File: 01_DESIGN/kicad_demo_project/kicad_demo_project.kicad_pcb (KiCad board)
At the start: 2 copper layers, 15 parts, among them J1 JP2, J2 0473460001, J3 JP8, J4 JP2, J5 JP8, U2 TPS7A4533DCQR, U3 STM32H745ZIT3, U6 ATMEGA324PA, U8 LM2596S-5, Y1 ECS-250-12-33Q-JES-TR, Y2 8MHz

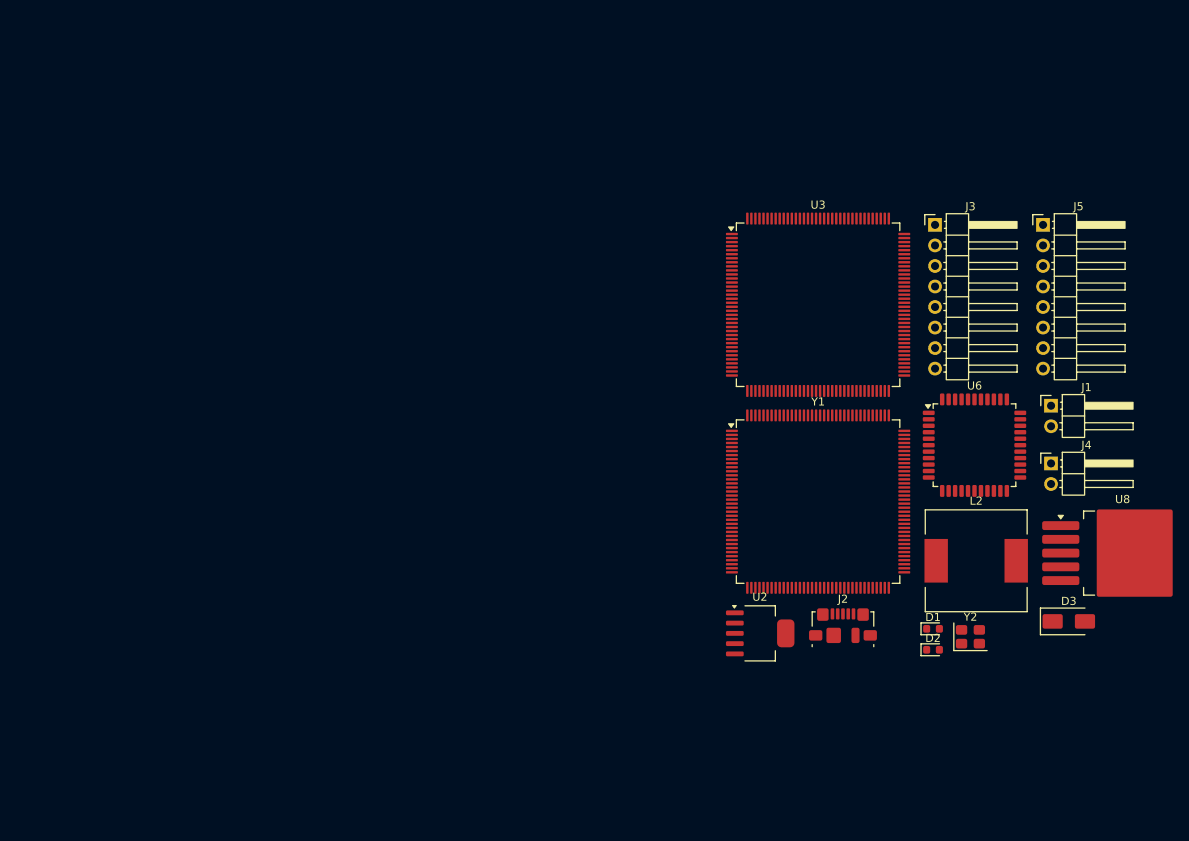
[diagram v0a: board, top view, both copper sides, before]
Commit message: Update schematic, PCB
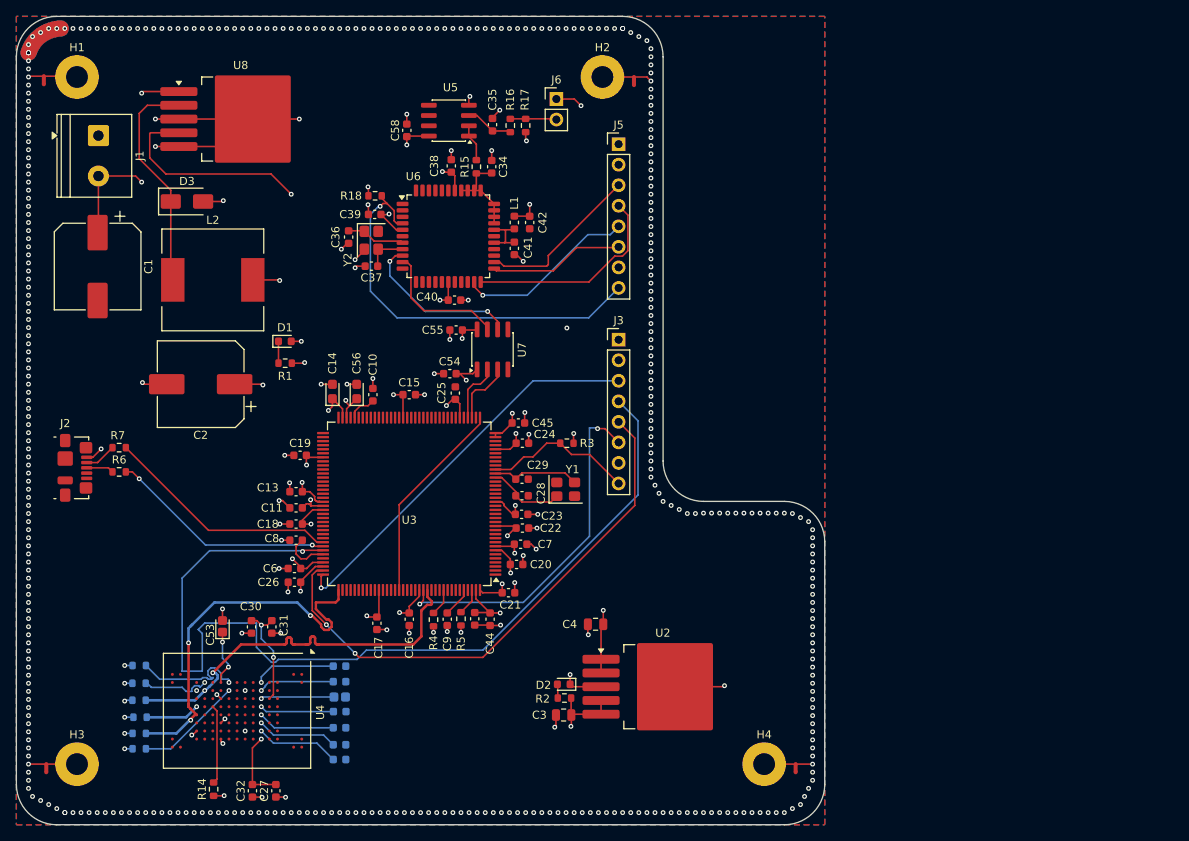
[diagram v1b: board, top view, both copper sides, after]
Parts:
- removed J4: JP2, Connector_PinHeader_2.54mm:PinHeader_1x02_P2.54mm_Horizontal
- added C1: 680uF, Capacitor_SMD:CP_Elec_10x10.5, F.Cu at (60.0, 74.0)
- added C10: 4.7uF/6.3V, Capacitor_SMD:C_0603_1608Metric, F.Cu at (94.1, 89.8)
- added C11: 0.1uF/6.3V, Capacitor_SMD:C_0603_1608Metric, F.Cu at (84.6, 103.8)
- added C13: 4.7uF/6.3V, Capacitor_SMD:C_0603_1608Metric, F.Cu at (84.6, 101.8)
- added C14: 4.7uF, Capacitor_Tantalum_SMD:CP_EIA-2012-15_AVX-P, F.Cu at (89.1, 89.4)
- added C15: 0.1uF/6.3V, Capacitor_SMD:C_0603_1608Metric, F.Cu at (98.6, 89.8)
- added C16: 0.1uF/6.3V, Capacitor_SMD:C_0603_1608Metric, F.Cu at (98.6, 117.6)
- added C17: 0.1uF/6.3V, Capacitor_SMD:C_0603_1608Metric, F.Cu at (94.6, 118.1)
- added C18: 0.1uF/6.3V, Capacitor_SMD:C_0603_1608Metric, F.Cu at (84.6, 105.8)
- added C19: 0.1uF/6.3V, Capacitor_SMD:C_0603_1608Metric, F.Cu at (85.1, 97.3)
- added C2: 220uF, Capacitor_SMD:CP_Elec_10x10.5, F.Cu at (72.8, 88.5)
- added C20: 0.1uF/6.3V, Capacitor_SMD:C_0603_1608Metric, F.Cu at (111.9, 110.8)
- added C21: 0.1uF/6.3V, Capacitor_SMD:C_0603_1608Metric, F.Cu at (110.9, 114.3)
- added C22: 0.1uF/6.3V, Capacitor_SMD:C_0603_1608Metric, F.Cu at (112.6, 106.3)
- added C23: 0.1uF/6.3V, Capacitor_SMD:C_0603_1608Metric, F.Cu at (112.5, 104.6)
- added C24: 0.1uF/6.3V, Capacitor_SMD:C_0603_1608Metric, F.Cu at (112.6, 95.8)
- added C25: 0.1uF/6.3V, Capacitor_SMD:C_0603_1608Metric, F.Cu at (104.3, 89.6)
- added C26: 0.1uF/6.3V, Capacitor_SMD:C_0603_1608Metric, F.Cu at (84.4, 113.0)
- added C27: 0.1uF/6.3V, Capacitor_SMD:C_0603_1608Metric, F.Cu at (82.1, 138.8)
- added C28: 16pF/6.3V, Capacitor_SMD:C_0603_1608Metric, F.Cu at (112.5, 102.3)
- added C29: 16pF/6.3V, Capacitor_SMD:C_0603_1608Metric, F.Cu at (112.5, 100.2)
- added C3: 10uF, Capacitor_SMD:C_0805_2012Metric, F.Cu at (117.7, 129.4)
- added C30: 0.1uF/6.3V, Capacitor_SMD:C_0603_1608Metric, F.Cu at (79.1, 118.5)
- added C31: 1uF/6.3V, Capacitor_SMD:C_0603_1608Metric, F.Cu at (81.6, 118.5)
- added C32: 0.1uF/6.3V, Capacitor_SMD:C_0603_1608Metric, F.Cu at (79.2, 138.8)
- added C34: 0.1uF/6.3V, Capacitor_SMD:C_0603_1608Metric, F.Cu at (108.8, 61.6)
- added C35: 0.1uF/6.3V, Capacitor_SMD:C_0603_1608Metric, F.Cu at (108.9, 56.4)
- added C36: 16pF/6.3V, Capacitor_SMD:C_0603_1608Metric, F.Cu at (91.1, 70.3)
- added C37: 16pF/6.3V, Capacitor_SMD:C_0603_1608Metric, F.Cu at (93.9, 73.9)
- added C38: 0.1uF/6.3V, Capacitor_SMD:C_0603_1608Metric, F.Cu at (103.8, 61.5)
- added C39: 0.1uF/6.3V, Capacitor_SMD:C_0603_1608Metric, F.Cu at (94.3, 67.5)
- added C4: 10uF, Capacitor_SMD:C_0805_2012Metric, F.Cu at (121.7, 118.2)
- added C40: 0.1uF/6.3V, Capacitor_SMD:C_0603_1608Metric, F.Cu at (104.2, 78.1)
- added C41: 0.1uF/6.3V, Capacitor_SMD:C_0603_1608Metric, F.Cu at (111.6, 71.7)
- added C42: 0.1uF/6.3V, Capacitor_SMD:C_0603_1608Metric, F.Cu at (113.5, 68.5)
- added C43: 0.1uF/6.3V, Capacitor_SMD:CAP_C_1608X80, F.Cu at (106.7, 117.5)
- added C44: 0.1uF/6.3V, Capacitor_SMD:C_0603_1608Metric, F.Cu at (108.6, 117.6)
- added C45: 0.1uF/6.3V, Capacitor_SMD:C_0603_1608Metric, F.Cu at (112.1, 93.3)
- added C46: 0.1uF/6.3V, Capacitor_SMD:C_0603_1608Metric, B.Cu at (90.0, 134.9)
- added C47: 0.1uF/6.3V, Capacitor_SMD:C_0603_1608Metric, B.Cu at (90.0, 133.1)
- added C48: 0.1uF/6.3V, Capacitor_SMD:C_0603_1608Metric, B.Cu at (90.0, 131.0)
- added C49: 0.1uF/6.3V, Capacitor_SMD:C_0603_1608Metric, B.Cu at (90.0, 129.0)
- added C50: 0.1uF/6.3V, Capacitor_SMD:C_0603_1608Metric, B.Cu at (90.0, 125.3)
- added C51: 0.1uF/6.3V, Capacitor_SMD:C_0603_1608Metric, B.Cu at (90.0, 123.4)
- added C52: 4.7uF, Capacitor_Tantalum_SMD:CP_EIA-1608-10_AVX-L, B.Cu at (90.0, 127.2)
- added C53: 4.7uF, Capacitor_Tantalum_SMD:CP_EIA-1608-10_AVX-L, F.Cu at (75.5, 118.5)
- added C54: 0.1uF/6.3V, Capacitor_SMD:C_0603_1608Metric, F.Cu at (103.6, 87.2)
- added C55: 0.1uF/6.3V, Capacitor_SMD:C_0603_1608Metric, F.Cu at (104.4, 81.8)
- added C56: 4.7uF, Capacitor_Tantalum_SMD:CP_EIA-2012-15_AVX-P, F.Cu at (92.1, 89.4)
- added C58: 0.1uF/6.3V, Capacitor_SMD:C_0603_1608Metric, F.Cu at (98.3, 57.1)
- added C6: 0.1uF/6.3V, Capacitor_SMD:C_0603_1608Metric, F.Cu at (84.4, 111.3)
- added C7: 0.1uF/6.3V, Capacitor_SMD:C_0603_1608Metric, F.Cu at (112.4, 108.3)
- added C8: 4.7uF/6.3V, Capacitor_SMD:C_0603_1608Metric, F.Cu at (84.6, 107.8)
- added C9: 4.7uF/6.3V, Capacitor_SMD:C_0603_1608Metric, F.Cu at (103.3, 117.6)
- added H1: MountingHole_Pad, MountingHole:MountingHole_2.7mm_M2.5_Pad, F.Cu at (57.5, 50.5)
- added H2: MountingHole_Pad, MountingHole:MountingHole_2.7mm_M2.5_Pad, F.Cu at (122.5, 50.5)
- added H3: MountingHole_Pad, MountingHole:MountingHole_2.7mm_M2.5_Pad, F.Cu at (57.5, 135.5)
- added H4: MountingHole_Pad, MountingHole:MountingHole_2.7mm_M2.5_Pad, F.Cu at (142.5, 135.5)
- added J6: Conn_01x02, Connector_PinHeader_2.54mm:PinHeader_1x02_P2.54mm_Vertical, F.Cu at (116.8, 53.2)
- added L1: 10uH/250mA, Inductor_SMD:L_0603_1608Metric, F.Cu at (111.6, 68.5)
- added NT1: NetTie_2, NetTie:NetTie-2_SMD_Pad0.5mm, F.Cu at (53.4, 50.9)
- added NT2: NetTie_2, NetTie:NetTie-2_SMD_Pad0.5mm, F.Cu at (126.4, 51.0)
- added NT3: NetTie_2, NetTie:NetTie-2_SMD_Pad0.5mm, F.Cu at (53.7, 136.0)
- added NT4: NetTie_2, NetTie:NetTie-2_SMD_Pad0.5mm, F.Cu at (146.4, 136.0)
- added R1: 1k, Resistor_SMD:R_0603_1608Metric, F.Cu at (83.2, 85.9)
- added R10: 10k, Resistor_SMD:R_0603_1608Metric, B.Cu at (65.2, 125.5)
- added R11: 10k, Resistor_SMD:R_0603_1608Metric, B.Cu at (65.2, 123.3)
- added R12: 10k, Resistor_SMD:R_0603_1608Metric, B.Cu at (65.3, 129.7)
- added R13: 10k, Resistor_SMD:R_0603_1608Metric, B.Cu at (65.2, 131.7)
- added R14: 4.7k, Resistor_SMD:R_0603_1608Metric, F.Cu at (74.4, 138.6)
- added R15: 22R, Resistor_SMD:R_0603_1608Metric, F.Cu at (106.9, 61.6)
- added R16: 22R, Resistor_SMD:R_0603_1608Metric, F.Cu at (111.1, 56.5)
- added R17: 10k, Resistor_SMD:R_0603_1608Metric, F.Cu at (113.0, 56.5)
- added R18: 4.7k, Resistor_SMD:R_0603_1608Metric, F.Cu at (94.4, 65.2)
- added R2: 1k, Resistor_SMD:R_0603_1608Metric, F.Cu at (117.8, 127.3)
- added R3: 4.7k, Resistor_SMD:R_0603_1608Metric, F.Cu at (118.1, 95.8)
- added R4: 4.7k, Resistor_SMD:R_0603_1608Metric, F.Cu at (101.6, 117.6)
- added R5: 4.7k, Resistor_SMD:R_0603_1608Metric, F.Cu at (105.0, 117.5)
- added R6: 0R/DNP, Resistor_SMD:R_0603_1608Metric, F.Cu at (62.7, 99.3)
- added R7: 0R/DNP, Resistor_SMD:R_0603_1608Metric, F.Cu at (62.7, 96.3)
- added R8: 10k, Resistor_SMD:R_0603_1608Metric, B.Cu at (65.2, 127.6)
- added R9: 10k, Resistor_SMD:R_0603_1608Metric, B.Cu at (65.2, 133.6)
- added U4: MTFC32GAZAQDW-AAT, Package_BGA:BGA-100_14x18mm_Layout10x17_P1mm, F.Cu at (77.3, 128.9)
- added U5: OPA2340, Package_SO:SOIC-8_3.9x4.9mm_P1.27mm, F.Cu at (103.5, 55.9)
- added U7: ISO7721DR, Package_SO:SOIC-8_3.9x4.9mm_P1.27mm, F.Cu at (108.9, 84.2)
- J1: value JP2 -> Screw_Terminal_01x02; footprint Connector_PinHeader_2.54mm:PinHeader_1x02_P2.54mm_Horizontal -> TerminalBlock_Phoenix:TerminalBlock_Phoenix_PT-1,5-2-5.0-H_1x02_P5.00mm_Horizontal
- J3, J5: value JP8 -> Conn_01x08; footprint Connector_PinHeader_2.54mm:PinHeader_1x08_P2.54mm_Horizontal -> Connector_PinHeader_2.54mm:PinHeader_1x08_P2.54mm_Vertical
- U2: footprint Package_TO_SOT_SMD:SOT-223-6 -> Package_TO_SOT_SMD:TO-263-5_TabPin3
- Y1: value ECS-250-12-33Q-JES-TR -> Crystal_GND24; footprint Package_QFP:LQFP-144_20x20mm_P0.5mm -> Crystal:Crystal_SMD_3225-4Pin_3.2x2.5mm
- Y2: value 8MHz -> Crystal_GND24
- moved J1 122.5 mm to (60.1, 57.8), turned to -90 degrees
- moved U8 121.6 mm to (77.8, 55.7)
- moved D3 120.8 mm to (71.1, 65.9)
- moved L2 100.6 mm to (74.3, 75.6)
- moved J2 97.0 mm to (57.2, 98.8), turned to -90 degrees
- moved Y2 88.9 mm to (93.9, 70.7), turned to -90 degrees
- moved D1 87.7 mm to (83.2, 83.2)
- moved U6 70.0 mm to (103.4, 70.2)
- moved U3 56.3 mm to (98.6, 103.3), turned to 180 degrees
- moved J5 53.4 mm to (124.5, 58.8)
- moved D2 45.9 mm to (117.7, 125.6), turned to 180 degrees
- moved J3 41.6 mm to (124.5, 83.0)
- moved Y1 31.3 mm to (118.0, 101.5)
- moved U2 13.7 mm to (130.0, 125.9)
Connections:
- J1 pad 1: +12V -> GND
- J1 pad 2: GND -> +12V
- J2 pad SH: (no net) -> unconnected-(J2-Shield-PadSH)_1
- L2 pad 2: Net-(C2-Pad1) -> +5V
- U3 pad 109: unconnected-(U3B-PC10-Pad109) -> MCU_eMMC_SDMMC2_CK
- U3 pad 131: /MCU/MCU_eMMC_SDMMC2_D3 -> MCU_eMMC_SDMMC2_D3
- U3 pad 29: /MCU/MCU_eMMC_SDMMC2_CK -> unconnected-(U3B-PC1-Pad29)
- U3 pad 37: /MCU/MCU_eMMC_SDMMC2_CMD -> /MCU/MCU_eMMC_SDMMC2_D2
- U3 pad 39: /MCU/MCU_ISO_UART2_TX -> MCU_ISO_UART2_TX
- U3 pad 40: /MCU/MCU_ISO_UART2_RX -> MCU_ISO_UART2_RX
- U6 pad 10: /AVR/AVR_ISO_UART0_TX -> AVR_ISO_UART0_TX
- U6 pad 9: /AVR/AVR_ISO_UART0_RX -> AVR_ISO_UART0_RX
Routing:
- net /POWER/SHIELDING: track 0.00 -> 1364.3 mm, vias 0 -> 381
- net +3.3V: track 0.00 -> 195.5 mm, vias 0 -> 48
- net /MCU/MCU_JTAG_TMS: track 0.00 -> 118.0 mm, vias 0 -> 1
- net +5V: track 0.00 -> 107.3 mm, vias 0 -> 15
- net GND: track 0.00 -> 105.2 mm, vias 0 -> 52
- net /MCU/MCU_JTAG_TCK: track 0.00 -> 67.3 mm, vias 0 -> 2
- net /AVR/AVR_JTAG_nRESET: track 0.00 -> 50.3 mm, vias 0 -> 1
- net /MCU/MCU_JTAG_TDI: track 0.00 -> 49.2 mm, vias 0 -> 1
- net MCU_eMMC_SDMMC2_D3: track 0.00 -> 48.4 mm, vias 0 -> 2
- net MCU_eMMC_SDMMC2_CK: track 0.00 -> 47.6 mm, vias 0 -> 3
- net /MCU/MCU_JTAG_TDO: track 0.00 -> 44.1 mm, vias 0 -> 2
- net /MCU/USB_2.0_D_N: track 0.00 -> 29.2 mm
- net /MCU/USB_2.0_D_P: track 0.00 -> 28.2 mm, vias 0 -> 2
- net Net-(D3-K): track 0.00 -> 27.6 mm
- net /AVR/AVR_JTAG_TMS: track 0.00 -> 25.9 mm
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- added copper zone on In2.Cu, net +12V
- added copper zone on In2.Cu, net +3.3V
- added copper zone on In2.Cu, net +5V
- added copper zone on B.Cu, net GND
- added copper zone on F.Cu, net GND
- added copper zone on In1.Cu, net GND
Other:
- board outline added: 100 x 100 mm
- copper layers 2 -> 4
